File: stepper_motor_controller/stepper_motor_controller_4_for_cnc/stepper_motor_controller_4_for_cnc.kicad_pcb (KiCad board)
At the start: 2 copper layers, 31 parts, among them U1 74LS74, U11 LM317_TO-220, U3 74LS136

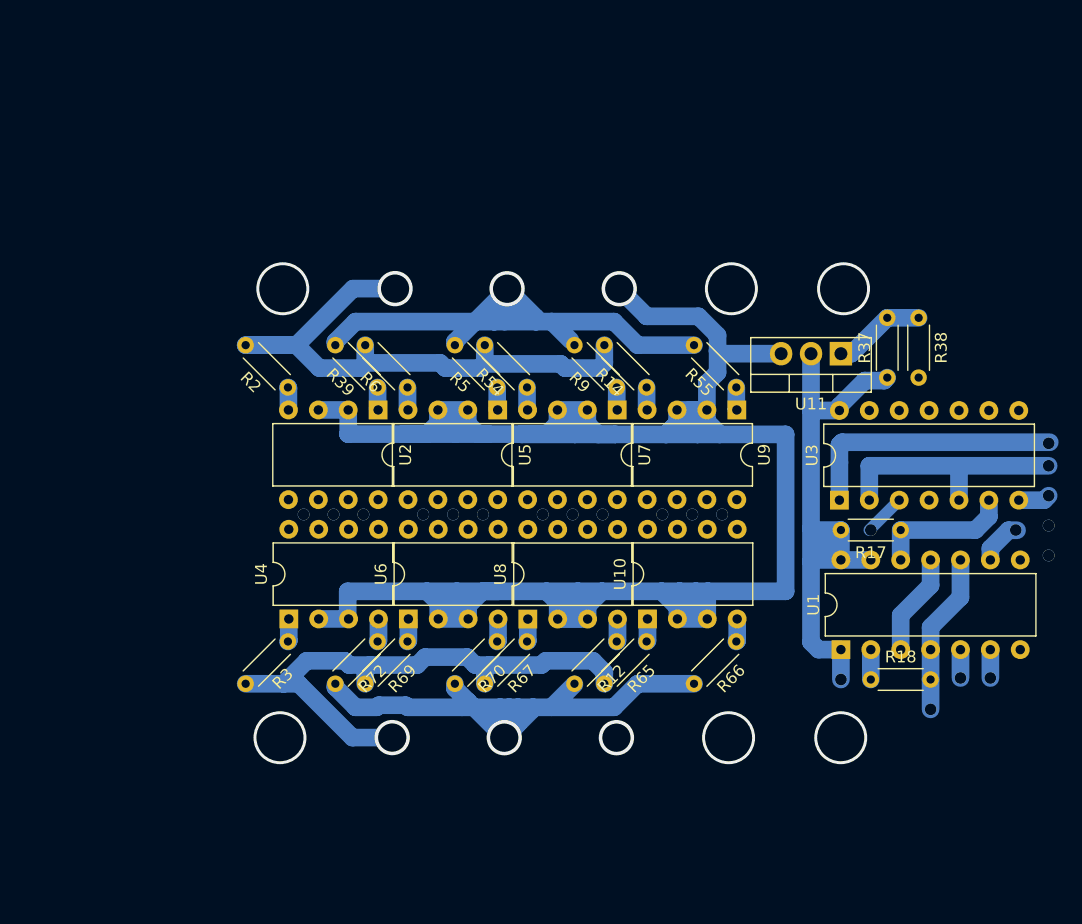
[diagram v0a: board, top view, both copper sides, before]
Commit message: rotate 90 degrees
reat
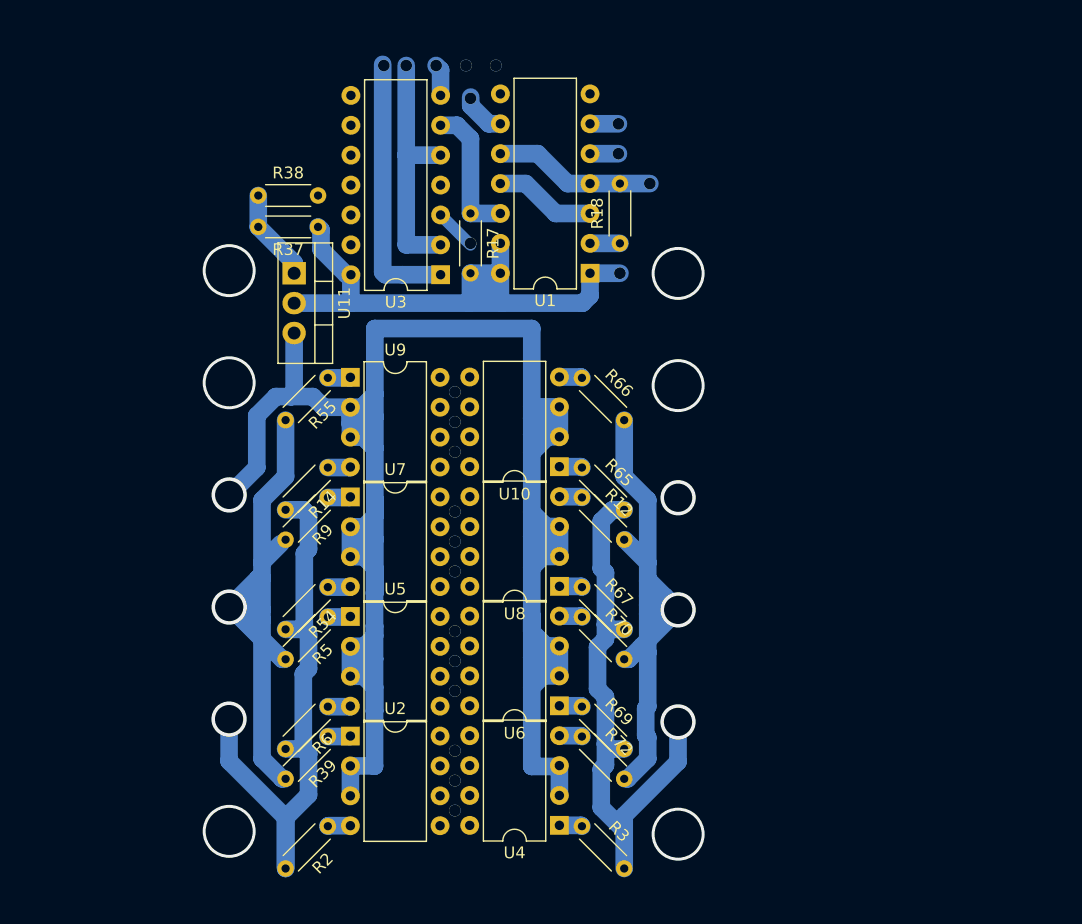
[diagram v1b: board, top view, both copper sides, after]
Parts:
- moved R38 57.1 mm to (21.6, -60.8), turned to 0 degrees
- moved R37 50.0 mm to (26.7, -58.1), turned to 180 degrees
- moved U11 47.0 mm to (24.7, -54.2), turned to -90 degrees
- moved R17 45.4 mm to (39.6, -59.3), turned to -90 degrees
- moved R18 42.8 mm to (52.3, -56.7), turned to 90 degrees
- moved U3 38.9 mm to (37.1, -54.1), turned to 180 degrees
- moved U1 38.4 mm to (49.8, -54.2), turned to 180 degrees
- moved R2 37.4 mm to (27.5, -7.22), turned to -135 degrees
- moved R55 34.7 mm to (27.5, -45.3), turned to -135 degrees
- moved U9 33.0 mm to (29.4, -45.4), turned to 0 degrees
- moved R39 30.0 mm to (27.5, -14.8), turned to -135 degrees
- moved R3 29.5 mm to (49.1, -7.22), turned to -45 degrees
- moved U4 28.9 mm to (47.2, -7.29), turned to 180 degrees
- moved R6 28.0 mm to (27.5, -17.4), turned to -135 degrees
- moved R14 27.9 mm to (27.5, -37.7), turned to -135 degrees
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
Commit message: move right
fdsaf
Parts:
- moved R12 13.6 mm to (35.5, -35.5)
- moved R17 13.6 mm to (26.0, -59.6)
- moved R3 13.6 mm to (35.5, -7.53)
- moved R65 13.6 mm to (35.5, -38.0)
- moved R66 13.6 mm to (35.5, -45.6)
- moved R67 13.6 mm to (35.5, -27.9)
- moved R69 13.6 mm to (35.5, -17.7)
- moved R70 13.6 mm to (35.5, -25.3)
- moved R72 13.6 mm to (35.5, -15.2)
- moved U10 13.6 mm to (33.6, -38.1)
- moved U3 13.6 mm to (23.5, -54.4)
- moved U4 13.6 mm to (33.6, -7.61)
- moved U6 13.6 mm to (33.6, -17.8)
- moved U8 13.6 mm to (33.6, -27.9)
- moved R14 13.6 mm to (13.9, -38.0)
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
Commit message: gerber
gerber
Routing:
- net GND: track 2.70 -> 803.9 mm
- net VCC: track 198.8 -> 216.2 mm
- net Net-(U1A-D): track 6.13 -> 2.55 mm
- net /C: track 48.2 -> 48.9 mm
